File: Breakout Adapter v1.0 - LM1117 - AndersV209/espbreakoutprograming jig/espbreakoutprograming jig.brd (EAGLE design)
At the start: 56 x 50 mm, 15 parts, among them X1 MINI-USB_SHIELD4P-85-32004-00X

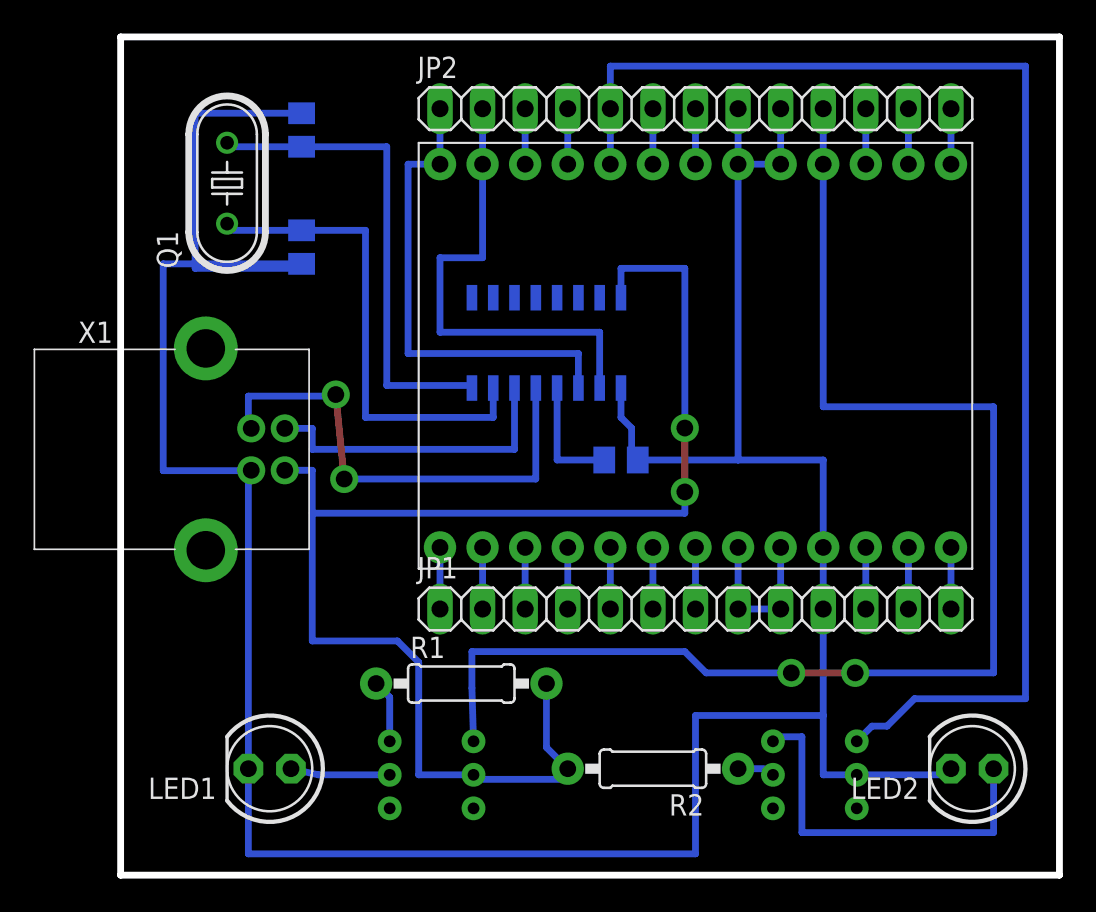
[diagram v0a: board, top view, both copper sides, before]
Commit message: update to programming jig
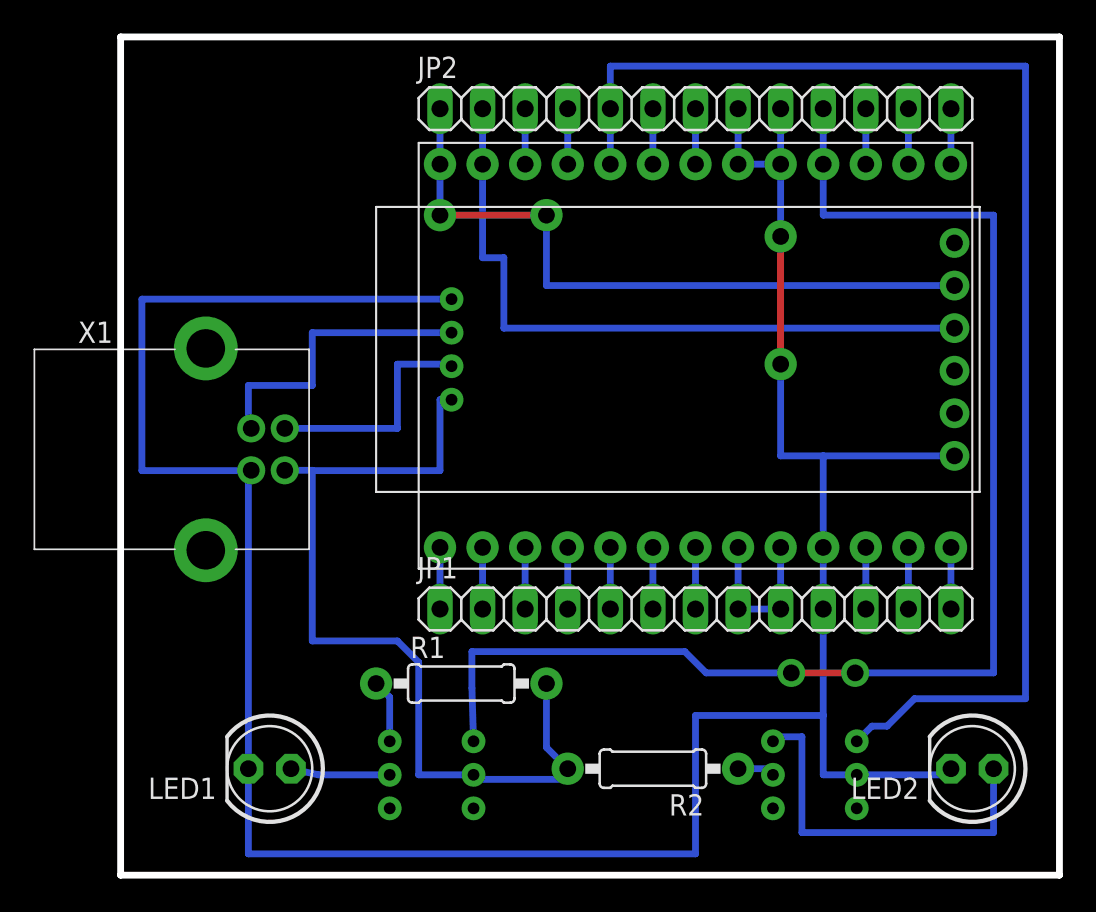
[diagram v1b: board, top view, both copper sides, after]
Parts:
- removed C1, C2, C3: (no value), rcl:C0805K
- removed Q1: (no value), adafruit:HC49U-V
- U$1: value CH340G -> USB-TTL; device usb-serial:SOIC16 -> mylib:USB_TTL
- moved U$1 13.5 mm to (15.2, 22.9), flipped to the top
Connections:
- removed net N$1: C1.1, Q1.1, U$1.7
- removed net N$2: C2.2, Q1.2, U$1.8
- removed net N$3: C3.2, U$1.4
- net D+: now also U$1.D+; no longer U$1.5
- net D-: now also U$1.D-; no longer U$1.6
- net GND: now also U$1.GND, U$1.GND1; no longer C1.2, C2.1, C3.1, U$1.1
- net RX: now also U$1.RXD; no longer U$1.3
- net TX: now also U$1.TXD; no longer U$1.2
- net VCC: now also U$1.VCC; no longer U$1.16
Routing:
- net VCC: track 83.2 -> 53.4 mm, vias 2 -> 0
- net N$2: track 29.2 -> 0.00 mm
- net N$1: track 29.2 -> 0.00 mm
- net GND: track 183.0 -> 164.8 mm, vias 0 -> 2
- net TX: track 28.7 -> 41.2 mm
- net RX: track 28.7 -> 41.2 mm, vias 0 -> 2
- net D+: track 29.3 -> 18.0 mm, vias 2 -> 0
- net N$3: track 7.10 -> 0.00 mm
- net D-: track 18.6 -> 13.9 mm
